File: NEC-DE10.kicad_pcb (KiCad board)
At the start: 2 copper layers, 110.5 x 72.4 mm, 12 parts, among them U3 74ALVC164245, U4 74ALVC164245, U5 74ALVC164245

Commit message: Added V35 board
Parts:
- added C10: 100nF, Capacitor_SMD:C_0603_1608Metric, F.Cu at (116.7, 113.0)
- added C11: 100nF, Capacitor_SMD:C_0603_1608Metric, F.Cu at (151.0, 103.5)
- added C12: 100nF, Capacitor_SMD:C_0603_1608Metric, F.Cu at (108.6, 140.9)
- added C13: 100nF, Capacitor_SMD:C_0603_1608Metric, F.Cu at (116.7, 132.9)
- added C14: 100nF, Capacitor_SMD:C_0603_1608Metric, F.Cu at (170.5, 151.8)
- added C15: 100nF, Capacitor_SMD:C_0603_1608Metric, F.Cu at (167.4, 112.1)
- added C16: 1uF, Capacitor_SMD:C_0603_1608Metric, F.Cu at (167.4, 110.3)
- added C17: 1uF, Capacitor_SMD:C_0603_1608Metric, F.Cu at (167.2, 151.8)
- added C18: 1uF, Capacitor_SMD:C_0603_1608Metric, F.Cu at (167.2, 64.3)
- added C8: 100nF, Capacitor_SMD:C_0603_1608Metric, F.Cu at (151.1, 100.2)
- added C9: 100nF, Capacitor_SMD:C_0603_1608Metric, F.Cu at (116.8, 117.1)
- added R1: 10k, Resistor_SMD:R_0603_1608Metric, F.Cu at (182.2, 129.7)
- added R10: 10k, Resistor_SMD:R_0603_1608Metric, F.Cu at (182.2, 149.2)
- added R11: 10k, Resistor_SMD:R_0603_1608Metric, F.Cu at (182.2, 147.2)
- added R12: 10k, Resistor_SMD:R_0603_1608Metric, F.Cu at (182.2, 145.8)
- added R13: 10k, Resistor_SMD:R_0603_1608Metric, F.Cu at (182.2, 144.0)
- added R14: 10k, Resistor_SMD:R_0603_1608Metric, F.Cu at (185.7, 142.3)
- added R15: 10k, Resistor_SMD:R_0603_1608Metric, F.Cu at (182.2, 142.3)
- added R16: 10k, Resistor_SMD:R_0603_1608Metric, F.Cu at (182.2, 139.8)
- added R17: 10k, Resistor_SMD:R_0603_1608Metric, F.Cu at (182.2, 134.8)
- added R18: 10k, Resistor_SMD:R_0603_1608Metric, F.Cu at (185.7, 132.3)
- added R19: 10k, Resistor_SMD:R_0603_1608Metric, F.Cu at (182.2, 132.3)
- added R2: 10k, Resistor_SMD:R_0603_1608Metric, F.Cu at (182.2, 127.2)
- added R20: 10k, Resistor_SMD:R_0603_1608Metric, F.Cu at (158.0, 151.8)
- added R21: 10k, Resistor_SMD:R_0603_1608Metric, F.Cu at (162.2, 151.8)
- added R22: 10k, Resistor_SMD:R_0603_1608Metric, F.Cu at (174.8, 153.5)
- added R23: 10k, Resistor_SMD:R_0603_1608Metric, F.Cu at (174.8, 151.8)
- added R24: 10k, Resistor_SMD:R_0603_1608Metric, F.Cu at (182.2, 119.6)
- added R25: 10k, Resistor_SMD:R_0603_1608Metric, F.Cu at (157.9, 112.1)
- added R26: 10k, Resistor_SMD:R_0603_1608Metric, F.Cu at (182.2, 152.8)
- added R27: 10k, Resistor_SMD:R_0603_1608Metric, F.Cu at (182.2, 117.1)
- added R28: 10k, Resistor_SMD:R_0603_1608Metric, F.Cu at (150.3, 112.1)
- added R3: 10k, Resistor_SMD:R_0603_1608Metric, F.Cu at (185.7, 127.2)
- added R4: 10k, Resistor_SMD:R_0603_1608Metric, F.Cu at (185.7, 124.6)
- added R5: 10k, Resistor_SMD:R_0603_1608Metric, F.Cu at (182.2, 124.6)
- added R6: 10k, Resistor_SMD:R_0603_1608Metric, F.Cu at (185.7, 122.1)
- added R7: 10k, Resistor_SMD:R_0603_1608Metric, F.Cu at (182.2, 122.1)
- added R8: 10k, Resistor_SMD:R_0603_1608Metric, F.Cu at (185.7, 119.6)
- added R9: 10k, Resistor_SMD:R_0603_1608Metric, F.Cu at (182.2, 151.0)
- added U10: 74ALVC164245, Package_SO:TSSOP-48_6.1x12.5mm_P0.5mm, F.Cu at (159.8, 102.5)
- added U6: 74ALVC164245, Package_SO:TSSOP-48_6.1x12.5mm_P0.5mm, F.Cu at (115.3, 140.8)
- added U7: 74ALVC164245, Package_SO:TSSOP-48_6.1x12.5mm_P0.5mm, F.Cu at (124.8, 116.0)
- added U8: ~, NEC-DE10:MODULE_P0496, F.Cu at (101.3, 155.5)
- added U9: ~, Package_LCC:PLCC-84_THT-Socket, F.Cu at (161.2, 117.0)
- moved C1 42.5 mm to (162.3, 30.6)
- moved C4 42.5 mm to (162.8, 36.0)
- moved U1 42.5 mm to (166.4, 44.2)
- moved U5 42.5 mm to (128.0, 32.5)
- moved C2 42.5 mm to (135.6, 30.6)
- moved C3 42.5 mm to (139.7, 73.2)
- moved C5 42.5 mm to (155.8, 67.8)
- moved C7 42.5 mm to (167.2, 62.1)
- moved U2 42.5 mm to (101.0, 82.6)
- moved U3 42.5 mm to (154.9, 33.0)
- moved U4 42.5 mm to (148.3, 70.7)
- moved C6 42.5 mm to (135.5, 35.4)
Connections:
- net /A16 renamed /V30/A16
- net /A17 renamed /V30/A17
- net /A18 renamed /V30/A18
- net /A19 renamed /V30/A19
- net /AD0 renamed /V30/AD0
- net /AD1 renamed /V30/AD1
- net /AD10 renamed /V30/AD10
- net /AD11 renamed /V30/AD11
- net /AD12 renamed /V30/AD12
- net /AD13 renamed /V30/AD13
- net /AD14 renamed /V30/AD14
- net /AD15 renamed /V30/AD15
- net /AD2 renamed /V30/AD2
- net /AD3 renamed /V30/AD3
- net /AD4 renamed /V30/AD4
- net /AD5 renamed /V30/AD5
- net /AD6 renamed /V30/AD6
- net /AD7 renamed /V30/AD7
- net /AD8 renamed /V30/AD8
- net /AD9 renamed /V30/AD9
- net /ASTB renamed /V30/ASTB
- net /BUF~{R}/W renamed /V30/BUF~{R}/W
- net /CLK renamed /V30/CLK
- net /F_A16 renamed /V30/F_A16
- net /F_A17 renamed /V30/F_A17
- net /F_A18 renamed /V30/F_A18
- net /F_A19 renamed /V30/F_A19
- net /F_AD0 renamed /V30/F_AD0
- net /F_AD1 renamed /V30/F_AD1
- net /F_AD10 renamed /V30/F_AD10
- net /F_AD11 renamed /V30/F_AD11
- net /F_AD12 renamed /V30/F_AD12
- net /F_AD13 renamed /V30/F_AD13
- net /F_AD14 renamed /V30/F_AD14
- net /F_AD15 renamed /V30/F_AD15
- net /F_AD2 renamed /V30/F_AD2
- net /F_AD3 renamed /V30/F_AD3
- net /F_AD4 renamed /V30/F_AD4
- net /F_AD5 renamed /V30/F_AD5
- net /F_AD6 renamed /V30/F_AD6
- net /F_AD7 renamed /V30/F_AD7
- net /F_AD8 renamed /V30/F_AD8
- net /F_AD9 renamed /V30/F_AD9
- net /F_AD_DIR renamed /V30/F_AD_DIR
- net /F_ASTB renamed /V30/F_ASTB
- net /F_BUF~{R}/W renamed /V30/F_BUF~{R}/W
- net /F_CLK renamed /V30/F_CLK
- net /F_INT renamed /V30/F_INT
- net /F_NMI renamed /V30/F_NMI
- net /F_READY renamed /V30/F_READY
- net /F_RESET renamed /V30/F_RESET
- net /F_S/~{LG} renamed /V30/F_S/~{LG}
- net /F_~{BUFEN} renamed /V30/F_~{BUFEN}
- net /F_~{INTAK} renamed /V30/F_~{INTAK}
- net /F_~{IO}/M renamed /V30/F_~{IO}/M
- net /F_~{POLL} renamed /V30/F_~{POLL}
- net /F_~{RD} renamed /V30/F_~{RD}
- net /F_~{UBE} renamed /V30/F_~{UBE}
- net /F_~{WR} renamed /V30/F_~{WR}
- net /INT renamed /V30/INT
- net /NMI renamed /V30/NMI
- net /READY renamed /V30/READY
- net /RESET renamed /V30/RESET
- net /S/~{LG} renamed /V30/S/~{LG}
- net /~{BUFEN} renamed /V30/~{BUFEN}
- net /~{INTAK} renamed /V30/~{INTAK}
- net /~{IO}/M renamed /V30/~{IO}/M
- net /~{POLL} renamed /V30/~{POLL}
- net /~{RD} renamed /V30/~{RD}
- net /~{UBE} renamed /V30/~{UBE}
- net /~{WR} renamed /V30/~{WR}
- U2 pad JP1_11: +5V -> unconnected-(U2A-5V_JP1-PadJP1_11)
- U2 pad JP1_29: +3.3V -> unconnected-(U2A-3.3V_JP1-PadJP1_29)
- U2 pad JP7_27: /F_HLDAK -> unconnected-(U2C-GPIO1_24-PadJP7_27)
- U4 pad 19: /HLDAK -> GND
- U4 pad 30: /F_HLDAK -> GND
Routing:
- net +5V: track 142.8 -> 358.3 mm, vias 7 -> 15
- net +3.3V: track 88.8 -> 294.4 mm, vias 3 -> 4
- net GND: track 58.5 -> 138.1 mm, vias 36 -> 93
- net /V35/R/~{W}: track 0.00 -> 56.4 mm, vias 0 -> 1
- net /V35/~{IOSTB}: track 0.00 -> 53.3 mm, vias 0 -> 1
- net /V35/~{MSTB}: track 0.00 -> 52.0 mm, vias 0 -> 1
- net /V35/N/~{S}: track 0.00 -> 49.6 mm
- net /V35/~{MREQ}: track 0.00 -> 48.9 mm, vias 0 -> 1
- net /V35/F_D_DIR: track 0.00 -> 46.0 mm, vias 0 -> 2
- net /V35/F_~{IOSTB}: track 0.00 -> 43.7 mm
- net /V35/F_~{MREQ}: track 0.00 -> 41.9 mm
- net /V35/A11: track 0.00 -> 41.4 mm
- net /V35/~{INTP0}: track 0.00 -> 40.5 mm
- net /V35/F_R/~{W}: track 0.00 -> 40.5 mm
- net /V35/A10: track 0.00 -> 39.6 mm
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- added copper zone on F.Cu, net +5V
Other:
- board size 110.5 x 72.4 mm -> 110.4 x 144.7 mm

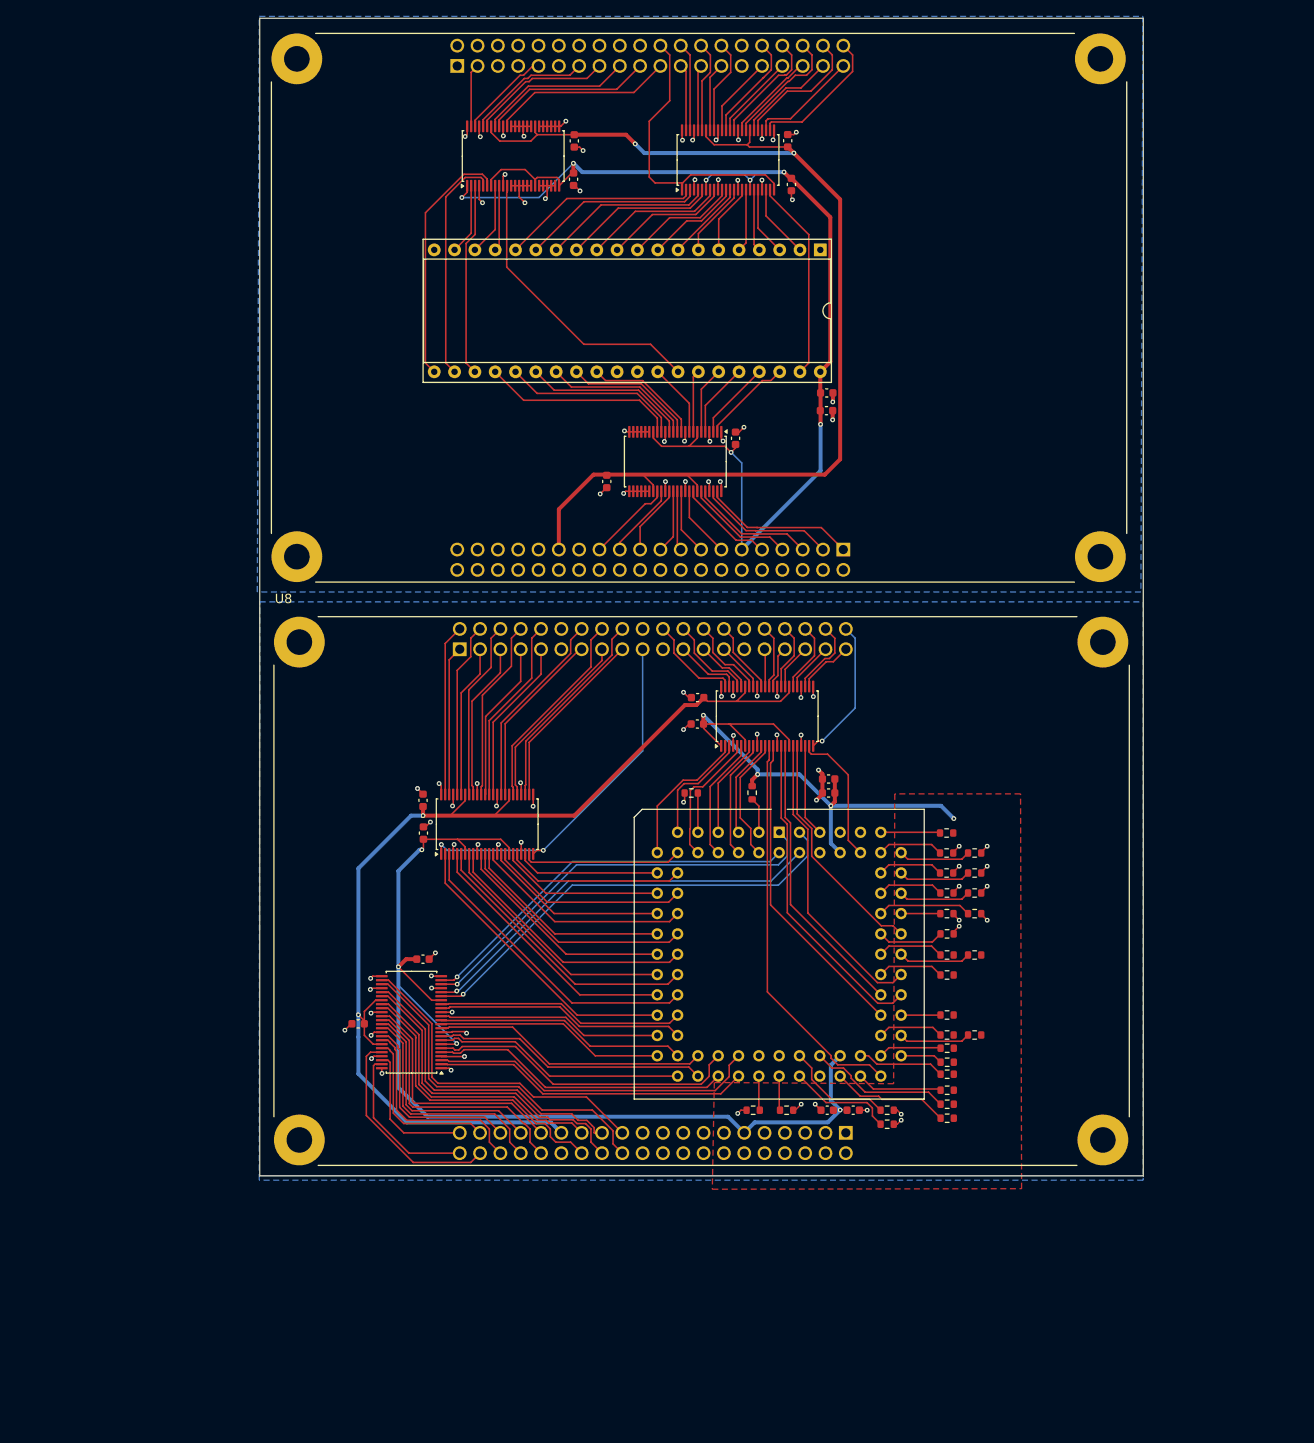
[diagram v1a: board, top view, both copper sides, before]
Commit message: Power tweaks. Revision 1 production submitted
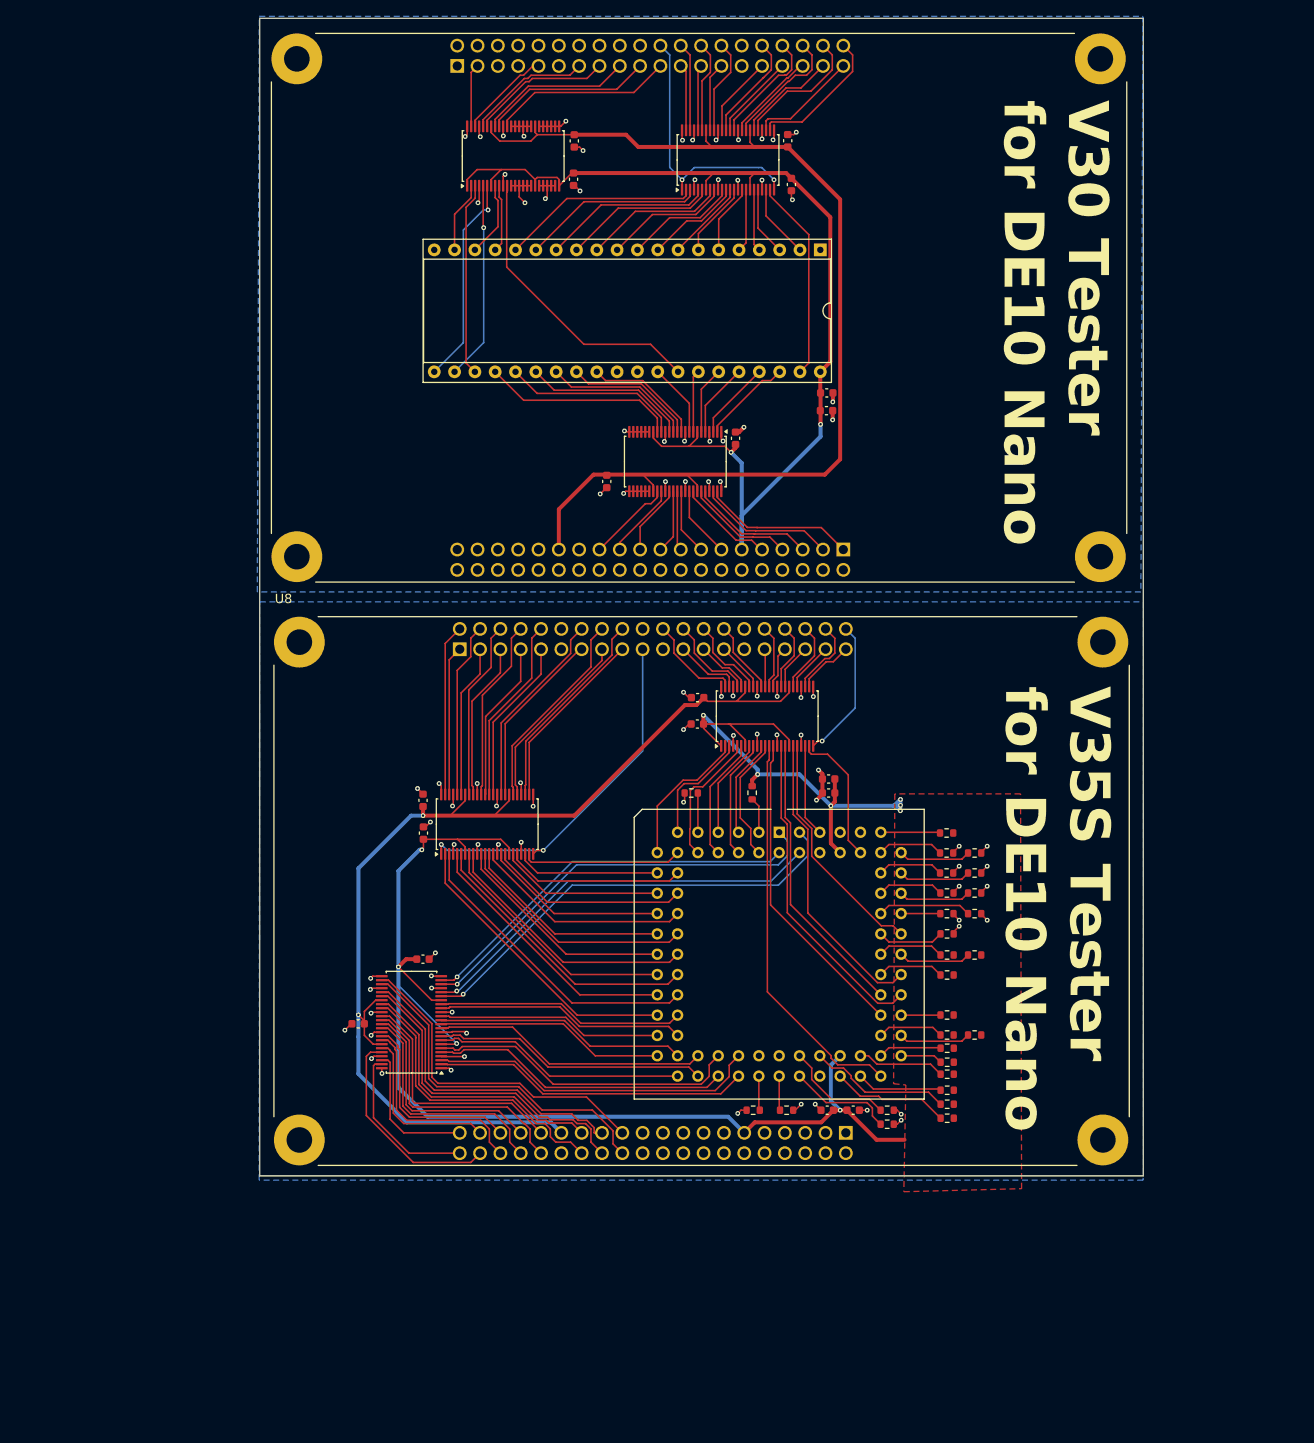
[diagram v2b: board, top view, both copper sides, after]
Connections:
- U2 pad SH1: (no net) -> GND
- U2 pad SH2: (no net) -> GND
- U2 pad SH3: (no net) -> GND
- U2 pad SH4: (no net) -> GND
- U8 pad SH1: (no net) -> GND
- U8 pad SH2: (no net) -> GND
- U8 pad SH3: (no net) -> GND
- U8 pad SH4: (no net) -> GND
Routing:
- net +5V: track 358.3 -> 345.4 mm, vias 15 -> 12
- net +3.3V: track 294.4 -> 284.5 mm, vias 4 -> 2
- net /V30/RESET: track 31.1 -> 26.4 mm, vias 0 -> 1
- net /V30/READY: track 28.9 -> 24.8 mm, vias 0 -> 1
- net /V30/F_AD_DIR: track 36.4 -> 33.1 mm, vias 0 -> 2
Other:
- board text added: "V30 Tester for DE10 Nano"
- board text added: "V35S Tester for DE10 Nano"

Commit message: Adding power control Moving board around for heat issues
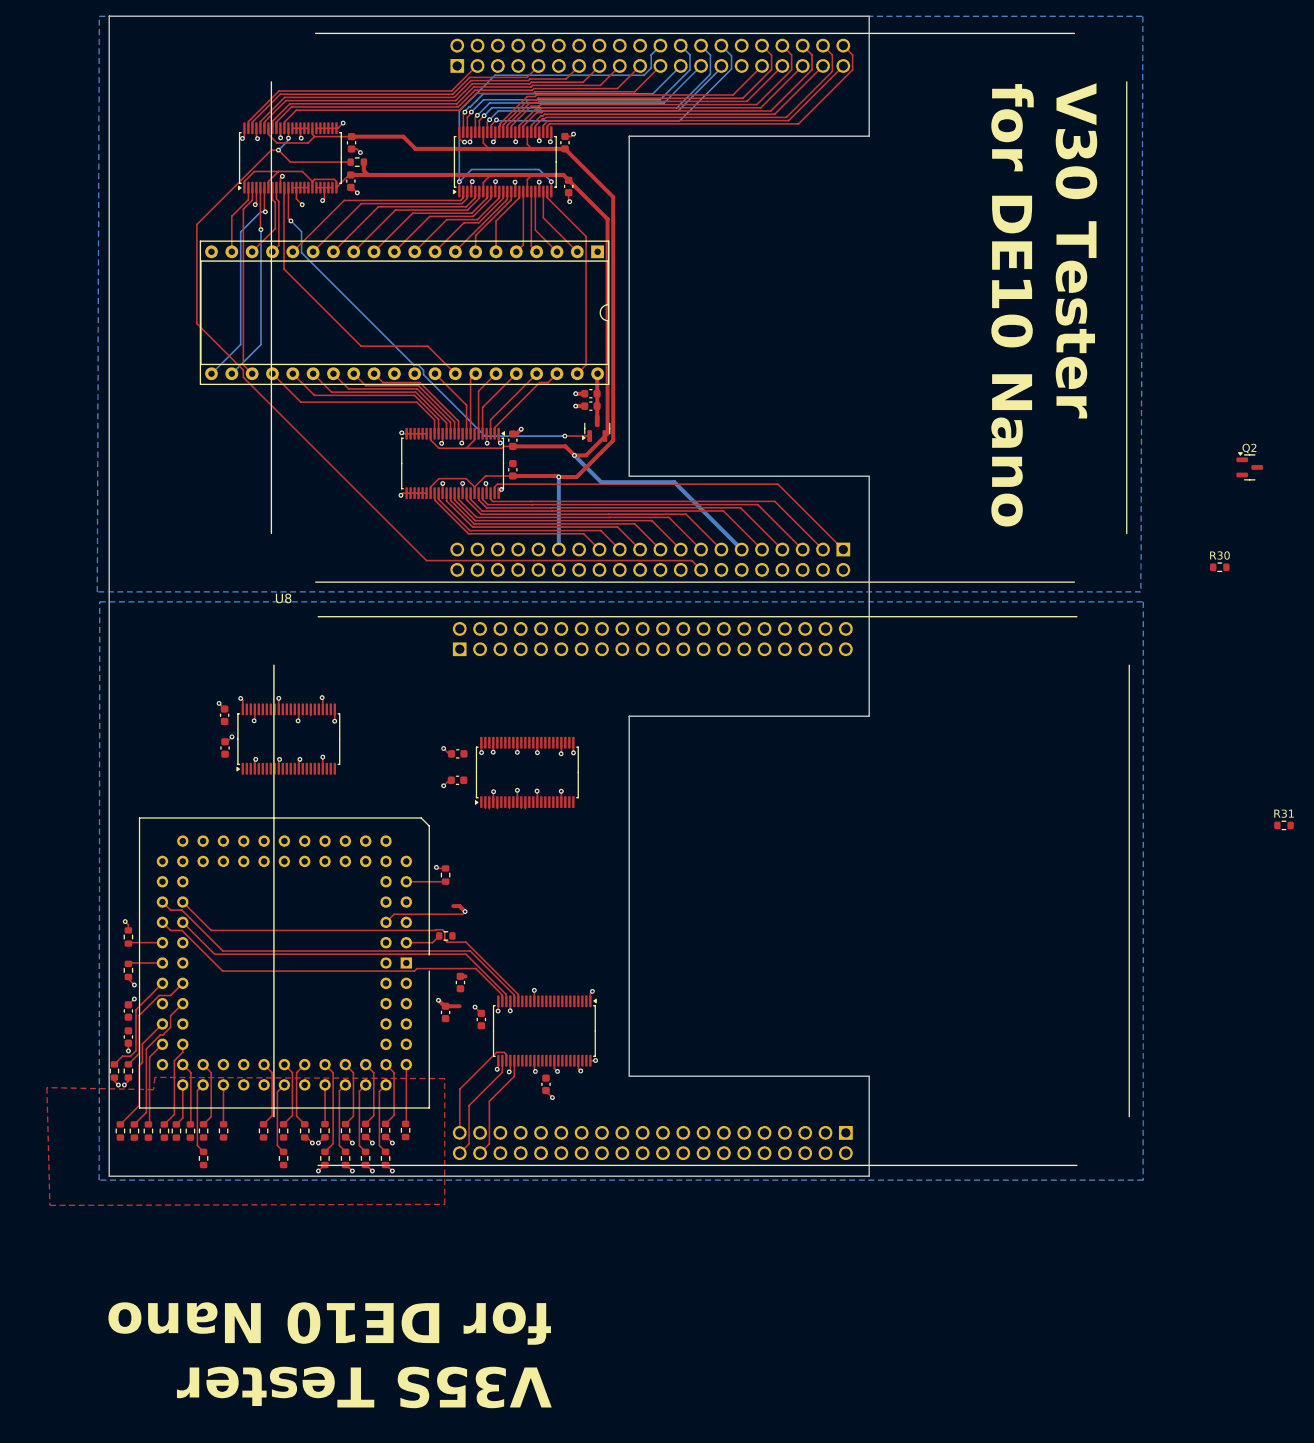
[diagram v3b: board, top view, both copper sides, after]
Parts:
- added Q1: SI2301CDS, Package_TO_SOT_SMD:SOT-23, F.Cu at (138.5, 66.5)
- added Q2: SI2301CDS, Package_TO_SOT_SMD:SOT-23, F.Cu at (220.1, 71.4)
- added R29: 10k, Resistor_SMD:R_0603_1608Metric, F.Cu at (108.5, 33.2)
- added R30: 10k, Resistor_SMD:R_0603_1608Metric, F.Cu at (216.3, 83.9)
- added R31: 10k, Resistor_SMD:R_0603_1608Metric, F.Cu at (224.3, 116.2)
- moved R26 103.4 mm to (78.9, 154.3), turned to 90 degrees
- moved R9 101.7 mm to (80.7, 154.3), turned to 90 degrees
- moved R10 100.0 mm to (82.4, 154.3), turned to 90 degrees
- moved R11 98.1 mm to (84.4, 154.3), turned to 90 degrees
- moved R14 97.6 mm to (89.3, 157.8), turned to 90 degrees
- moved R22 96.8 mm to (78.2, 146.8), turned to 90 degrees
- moved R12 96.7 mm to (85.9, 154.3), turned to 90 degrees
- moved R13 95.2 mm to (87.7, 154.3), turned to 90 degrees
- moved R23 95.0 mm to (79.9, 146.8), turned to 90 degrees
- moved R15 93.7 mm to (89.3, 154.3), turned to 90 degrees
- moved R16 91.6 mm to (91.8, 154.3), turned to 90 degrees
- moved C14 91.1 mm to (79.9, 142.6), turned to -90 degrees
- moved R18 90.0 mm to (99.3, 157.8), turned to 90 degrees
- moved C17 88.2 mm to (79.9, 139.3), turned to 90 degrees
- moved R17 87.6 mm to (96.8, 154.3), turned to 90 degrees
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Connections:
- C18 pad 1: +5V -> Net-(Q1-D)
- C7 pad 1: +5V -> Net-(Q1-D)
- U1 pad 40: +5V -> Net-(Q1-D)
- U10 pad 1: +5V -> /V35/F_P_DIR
- U10 pad 19: /V35/~{INTP2} -> /V35/~{CHIP_ENABLE}
- U10 pad 24: /V35/F_P_DIR -> +5V
- U10 pad 30: /V35/F_~{INTP2} -> /V35/~{F_CHIP_ENABLE}
- U2 pad JP7_16: unconnected-(U2C-GPIO1_13-PadJP7_16) -> /V30/~{F_CHIP_ENABLE}
- U5 pad 12: GND -> /V30/~{CHIP_ENABLE}
- U5 pad 37: GND -> /V30/~{F_CHIP_ENABLE}
- U6 pad 11: /V35/A7 -> /V35/A1
- U6 pad 12: /V35/A3 -> /V35/A5
- U6 pad 13: /V35/A5 -> /V35/A3
- U6 pad 14: /V35/A1 -> /V35/A7
- U6 pad 16: /V35/A2 -> /V35/A6
- U6 pad 17: /V35/A0 -> /V35/A4
- U6 pad 19: /V35/R/~{W} -> /V35/A9
- U6 pad 2: /V35/A10 -> /V35/~{MREQ}
- U6 pad 20: /V35/~{MSTB} -> /V35/A8
- U6 pad 22: /V35/~{IOSTB} -> /V35/A11
- U6 pad 23: /V35/~{MREQ} -> /V35/A10
- U6 pad 26: /V35/F_~{MREQ} -> /V35/F_A10
- U6 pad 27: /V35/F_~{IOSTB} -> /V35/F_A11
- U6 pad 29: /V35/F_~{MSTB} -> /V35/F_A8
- U6 pad 3: /V35/A11 -> /V35/~{IOSTB}
- U6 pad 30: /V35/F_R/~{W} -> /V35/F_A9
- U6 pad 32: /V35/F_A0 -> /V35/F_A4
- U6 pad 33: /V35/F_A2 -> /V35/F_A6
- U6 pad 35: /V35/F_A1 -> /V35/F_A7
- U6 pad 36: /V35/F_A5 -> /V35/F_A3
- U6 pad 37: /V35/F_A3 -> /V35/F_A5
- U6 pad 38: /V35/F_A7 -> /V35/F_A1
- U6 pad 40: /V35/F_A6 -> /V35/F_A2
- U6 pad 41: /V35/F_A4 -> /V35/F_A0
- U6 pad 43: /V35/F_A9 -> /V35/F_R/~{W}
- U6 pad 44: /V35/F_A8 -> /V35/F_~{MSTB}
- U6 pad 46: /V35/F_A11 -> /V35/F_~{IOSTB}
- U6 pad 47: /V35/F_A10 -> /V35/F_~{MREQ}
- U6 pad 5: /V35/A8 -> /V35/~{MSTB}
- U6 pad 6: /V35/A9 -> /V35/R/~{W}
- U6 pad 8: /V35/A4 -> /V35/A0
- U6 pad 9: /V35/A6 -> /V35/A2
- U8 pad JP1_36: /V35/F_~{INTP2} -> unconnected-(U8A-GPIO0_31-PadJP1_36)
- U8 pad JP7_16: unconnected-(U8C-GPIO1_13-PadJP7_16) -> /V35/~{F_CHIP_ENABLE}
- U9 pad 50: +5V -> Net-(Q2-D)
- U9 pad 62: /V35/~{INTP2} -> Net-(U9B-P13/~{INTP2})
- U9 pad 80: +5V -> Net-(Q2-D)
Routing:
- net +5V: track 345.4 -> 142.6 mm, vias 12 -> 2
- net +3.3V: track 284.5 -> 121.6 mm, vias 2 -> 1
- net /V30/~{F_CHIP_ENABLE}: track 0.00 -> 115.6 mm, vias 0 -> 2
- net /V35/R/~{W}: track 56.4 -> 0.00 mm, vias 1 -> 0
- net /V30/~{CHIP_ENABLE}: track 0.00 -> 54.7 mm, vias 0 -> 2
- net /V35/~{IOSTB}: track 53.3 -> 0.00 mm, vias 1 -> 0
- net /V35/~{MSTB}: track 52.0 -> 0.00 mm, vias 1 -> 0
- net /V35/N/~{S}: track 49.6 -> 0.00 mm
- net /V35/~{MREQ}: track 48.9 -> 0.00 mm, vias 1 -> 0
- net /V35/F_D_DIR: track 46.0 -> 0.00 mm, vias 2 -> 0
- net /V35/F_~{IOSTB}: track 43.7 -> 0.00 mm
- net /V35/F_~{MREQ}: track 41.9 -> 0.00 mm
- net /V35/~{INTP0}: track 40.5 -> 0.00 mm
- net /V35/F_R/~{W}: track 40.5 -> 0.00 mm
- net /V35/NMI: track 39.5 -> 0.00 mm
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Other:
- board size 110.4 x 144.7 mm -> 95 x 145 mm
